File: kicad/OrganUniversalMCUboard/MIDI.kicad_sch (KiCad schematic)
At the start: 15 parts, among them J3 MIDI IN, J4 MIDI OUTTHRU, Q1 Q_NPN, Q2 Q_NPN, U2 6N137

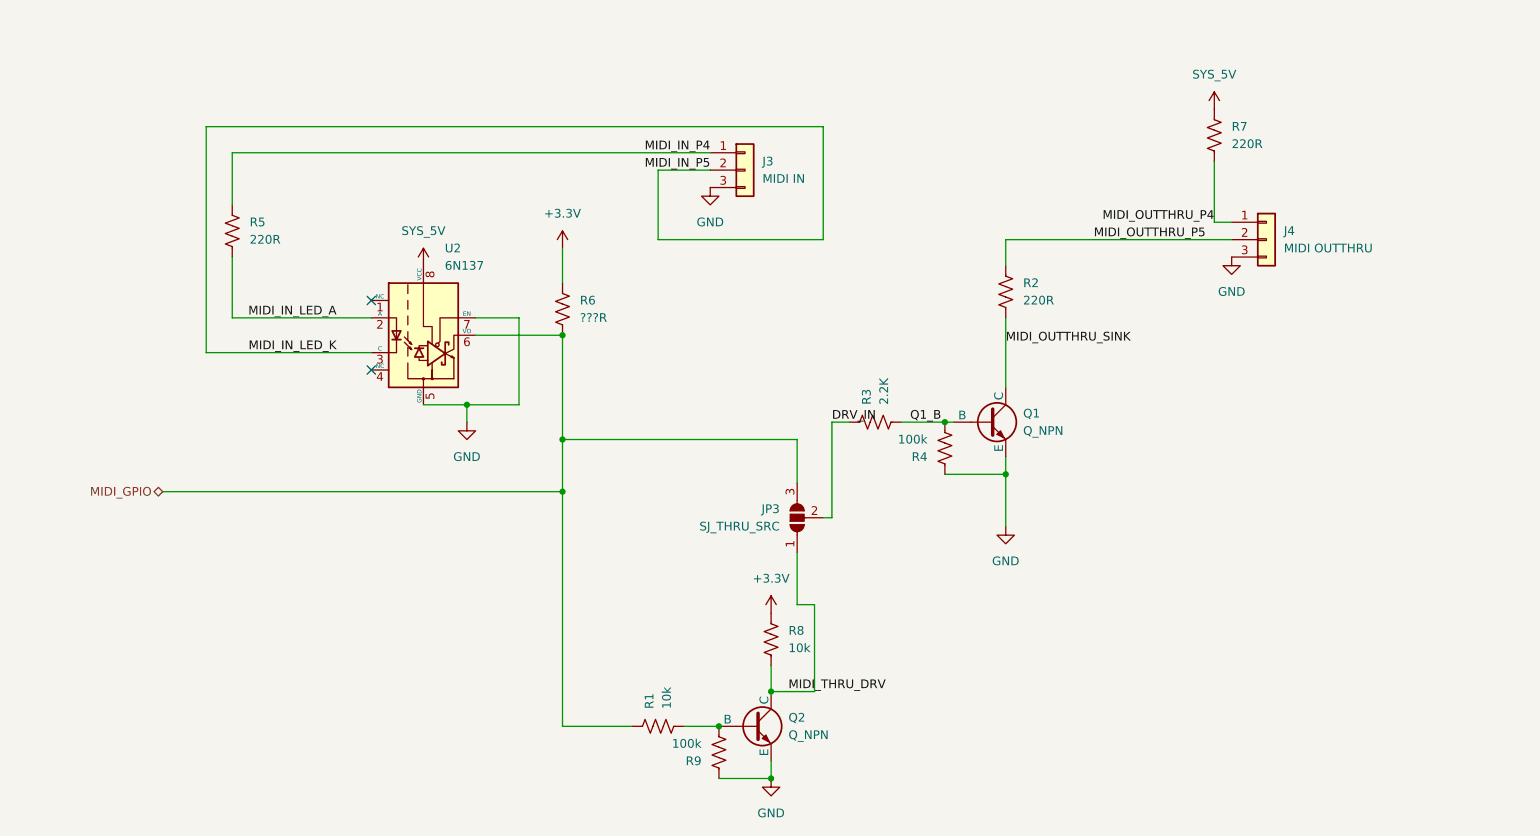
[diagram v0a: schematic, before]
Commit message: Finishing MCU board and lots of chimes updates
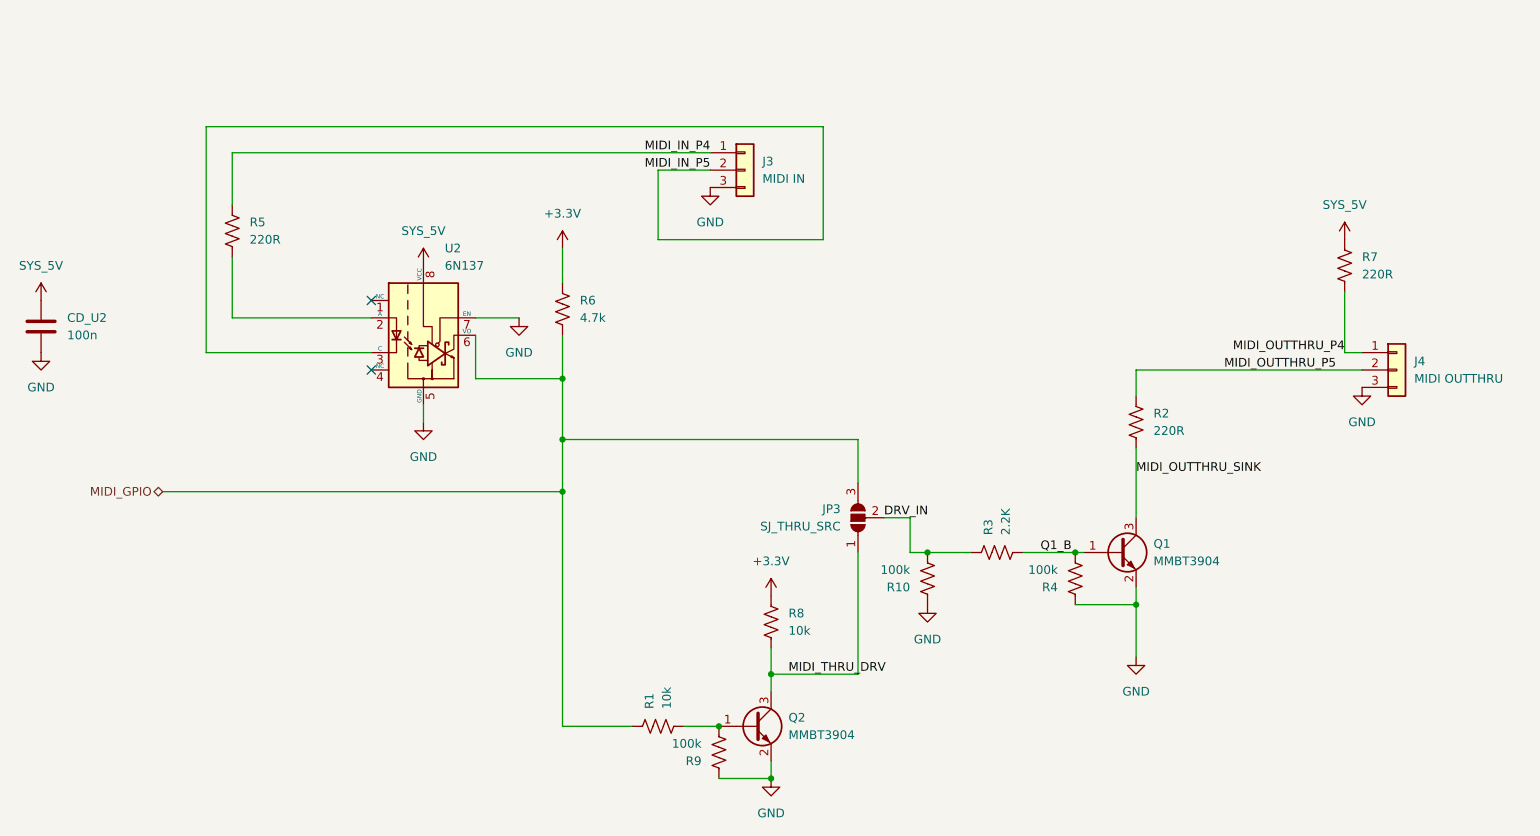
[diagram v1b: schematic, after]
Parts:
- removed Q1, Q2: Q_NPN, symbol Device:Q_NPN
- added CD_U2: 100n, Capacitor_SMD:C_0603_1608Metric, symbol Device:C
- added Q1, Q2: MMBT3904, Package_TO_SOT_SMD:SOT-23, symbol Transistor_BJT:MMBT3904
- added R10: 100k, Resistor_SMD:R_0603_1608Metric, symbol Device:R_US
- J3, J4: footprint (none) -> Connector_JST:JST_PH_B3B-PH-K_1x03_P2.00mm_Vertical
- JP3: footprint (none) -> Jumper:SolderJumper-3_P1.3mm_Open_RoundedPad1.0x1.5mm
- R1, R2, R3, R4, R5, R7, R8, R9: footprint (none) -> Resistor_SMD:R_0603_1608Metric
- R6: value ???R -> 4.7k; footprint (none) -> Resistor_SMD:R_0603_1608Metric
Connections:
- net DRV_IN: now also R10.2
- net GND: now also CD_U2.2, Q1.2 (E), Q2.2 (E), R10.1
- net MIDI_OUTTHRU_SINK: now also Q1.3 (C)
- net MIDI_THRU_DRV: now also Q2.3 (C)
- net Q1_B: now also Q1.1 (B)
- net SYS_5V: now also CD_U2.1
- net at R1.2, R9.2: now also Q2.1 (B)
- net MIDI_IN_LED_A: no longer names the net of R5.2, U2.2 (A)
- net MIDI_IN_LED_K renamed MIDI_IN_P5
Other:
- moved on the sheet: J4, JP3, R2, R3, R4, R7, R8

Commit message: Finalized v001 of MCU board for production
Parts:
- removed J3: MIDI IN, Connector_JST:JST_PH_B3B-PH-K_1x03_P2.00mm_Vertical, symbol Connector_Generic:Conn_01x03
- removed JP3: SJ_THRU_SRC, Jumper:SolderJumper-3_P1.3mm_Open_RoundedPad1.0x1.5mm, symbol Jumper:SolderJumper_3_Open
- removed R10: 100k, Resistor_SMD:R_0603_1608Metric, symbol Device:R_US
- added J3: MIDI IN, Connector_JST:JST_PH_B2B-PH-K_1x02_P2.00mm_Vertical, symbol Connector_Generic:Conn_01x02
- J4: value MIDI OUTTHRU -> MIDI_THRU
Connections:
- net DRV_IN is gone; now on net MIDI_THRU_DRV: R3.1
- net MIDI_IN_P4: now also J3.1 (Pin_1)
- net MIDI_IN_P5: now also J3.2 (Pin_2)
- net MIDI_OUTTHRU_P4 renamed MIDI_THRU_P4
- net MIDI_OUTTHRU_P5 renamed MIDI_THRU_P5
- net MIDI_THRU_P5: now also R2.2; no longer R2.1
- net MIDI_OUTTHRU_SINK renamed MIDI_THRU_SINK
- net MIDI_THRU_SINK: now also R2.1; no longer R2.2
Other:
- moved on the sheet: Q1, R2, R3, R4, R7
